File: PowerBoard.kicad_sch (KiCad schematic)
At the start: 113 parts, among them J1 XT90, J10 DEAN_T, J11 DEAN_T, J12 DEAN_T, J13 DEAN_T, J14 DEAN_T, J15 DEAN_T, J16 XT60, J17 XT60, J18 XT60, J19 XT60, J2 DEAN_T, J20 XT60, J21 XT60, J22 XT30, J23 XT30, J24 XT30, J25 XT30, J26 XT30, J27 XT30, J28 XT90, J29 XT30, J3 XT60, J30 XT30, J31 XT30, J32 Conn_01x02, J4 XT30, J5 XT90, J6 XT90, J7 XT90, J8 XT90, J9 XT90, Q1 IRF9540N, Q2 IRF9540N, Q3 BC817, Q4 BC817, Q5 IRF9540N, Q6 BC817, Q7 IRF9540N, Q8 BC817, U1 Pico, U2 LM317_TO-220

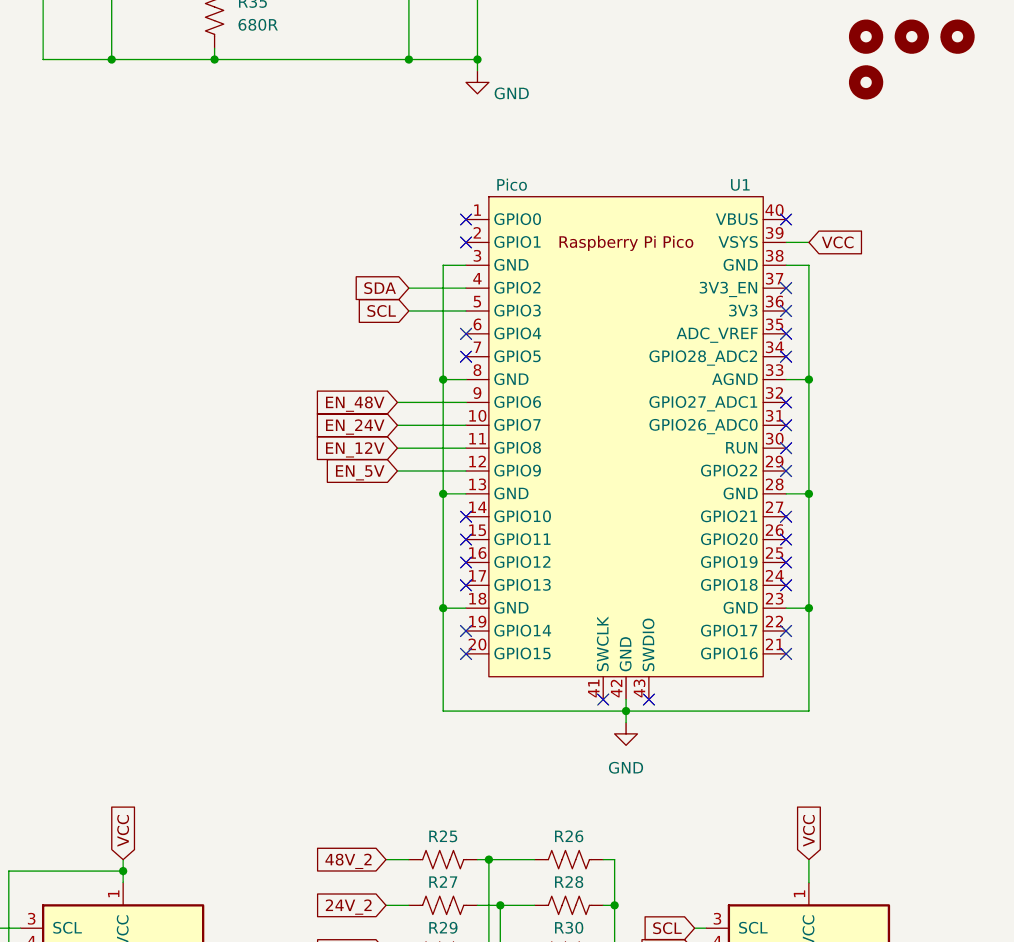
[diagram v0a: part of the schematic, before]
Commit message: added status leds
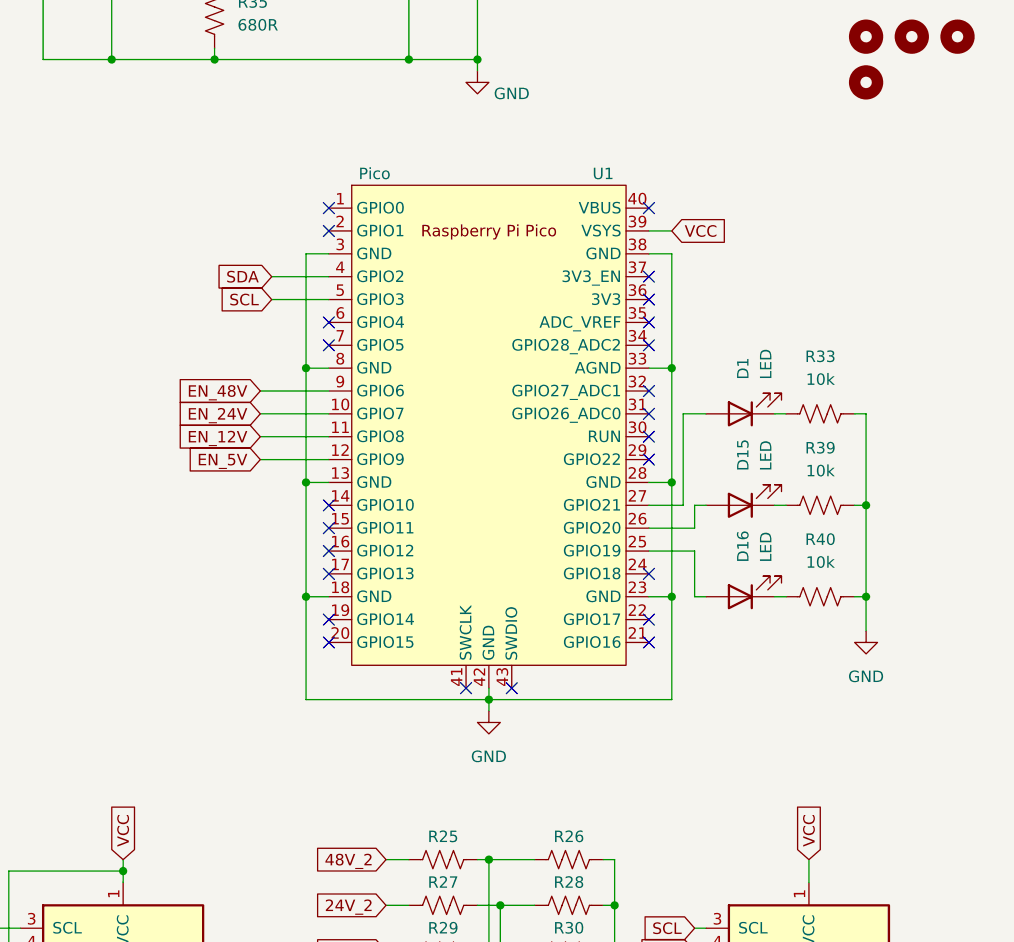
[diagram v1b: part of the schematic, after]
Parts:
- added D1, D15, D16: LED, Diode_SMD:D_1206_3216Metric, symbol Device:LED
- added R33, R39, R40: 10k, Resistor_SMD:R_1206_3216Metric, symbol Device:R_US
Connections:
- net GND: now also R33.2, R39.2, R40.2
- net at U1.25 (GPIO19): now also D16.2 (A)
- net at U1.26 (GPIO20): now also D15.2 (A)
- net at U1.27 (GPIO21): now also D1.2 (A)
- new net: D15.1 (K), R39.1
- new net: D16.1 (K), R40.1
- new net: D1.1 (K), R33.1
- no-connect marks 29 -> 26
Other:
- moved on the sheet: U1

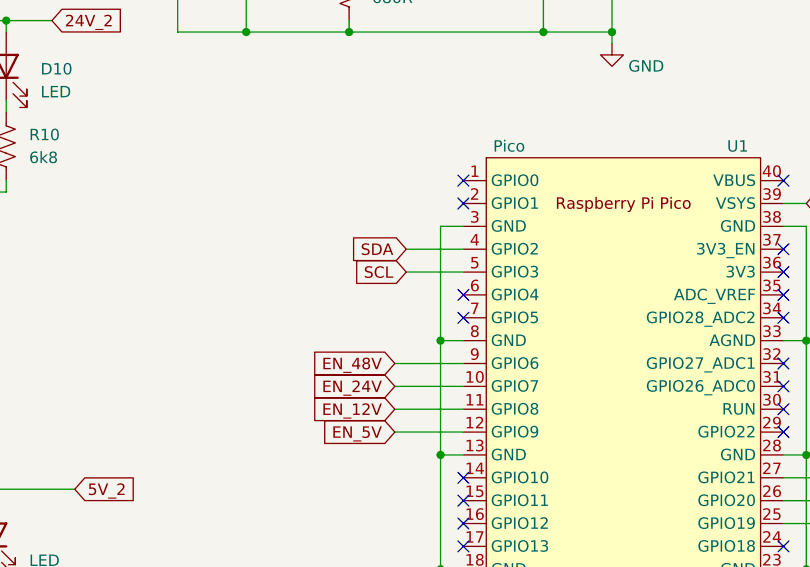
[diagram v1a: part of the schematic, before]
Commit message: changed i2c connection
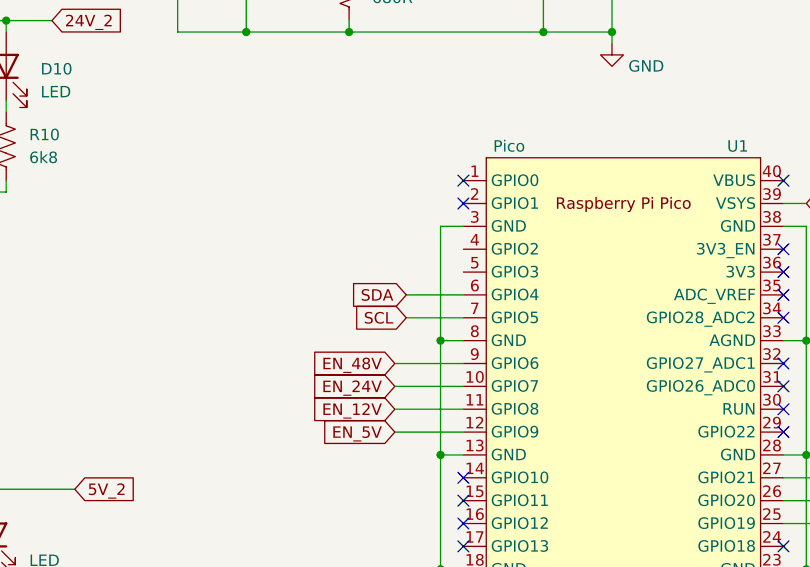
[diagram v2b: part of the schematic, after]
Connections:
- net SCL: now also U1.7 (GPIO5); no longer U1.5 (GPIO3)
- net SDA: now also U1.6 (GPIO4); no longer U1.4 (GPIO2)
- no-connect marks 26 -> 24
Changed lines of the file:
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@@
 	)
 	(no_connect
-		(at 208.28 71.12)
-	)
-	(no_connect
 		(at 243.84 104.14)
 	)
 	(no_connect
-		(at 208.28 68.58)
-	)
-	(no_connect
 		(at 243.84 76.2)
 	)
@@
 	(wire
 		(pts
-			(xy 201.93 66.04) (xy 208.28 66.04)
-		)
-		(stroke
-			(width 0)
-			(type default)
-		)
-	)
-	(wire
-		(pts
 			(xy 124.46 73.66) (xy 124.46 80.01)
 		)
@@
 	(wire
 		(pts
+			(xy 201.93 68.58) (xy 208.28 68.58)
+		)
+		(stroke
+			(width 0)
+			(type default)
+		)
+	)
+	(wire
+		(pts
 			(xy 205.74 110.49) (xy 226.06 110.49)
 		)
@@
 	(wire
 		(pts
-			(xy 201.93 63.5) (xy 208.28 63.5)
-		)
-		(stroke
-			(width 0)
-			(type default)
-		)
-	)
-	(wire
-		(pts
 			(xy 143.51 90.17) (xy 143.51 91.44)
 		)
@@
 	(wire
 		(pts
+			(xy 201.93 71.12) (xy 208.28 71.12)
+		)
+		(stroke
+			(width 0)
+			(type default)
+		)
+	)
+	(wire
+		(pts
 			(xy 44.45 27.94) (xy 41.91 27.94)
 		)
@@
 	(global_label "SCL"
 		(shape input)
-		(at 201.93 66.04 180)
+		(at 201.93 71.12 180)
 		(fields_autoplaced yes)
 		(effects
@@
 		)
 		(property "Intersheetrefs" "${INTERSHEET_REFS}"
-			(at 195.4372 66.04 0)
+			(at 195.4372 71.12 0)
 			(effects
 				(font
@@
 	(global_label "SDA"
 		(shape input)
-		(at 201.93 63.5 180)
+		(at 201.93 68.58 180)
 		(fields_autoplaced yes)
 		(effects
@@
 		)
 		(property "Intersheetrefs" "${INTERSHEET_REFS}"
-			(at 195.3767 63.5 0)
+			(at 195.3767 68.58 0)
 			(effects
 				(font

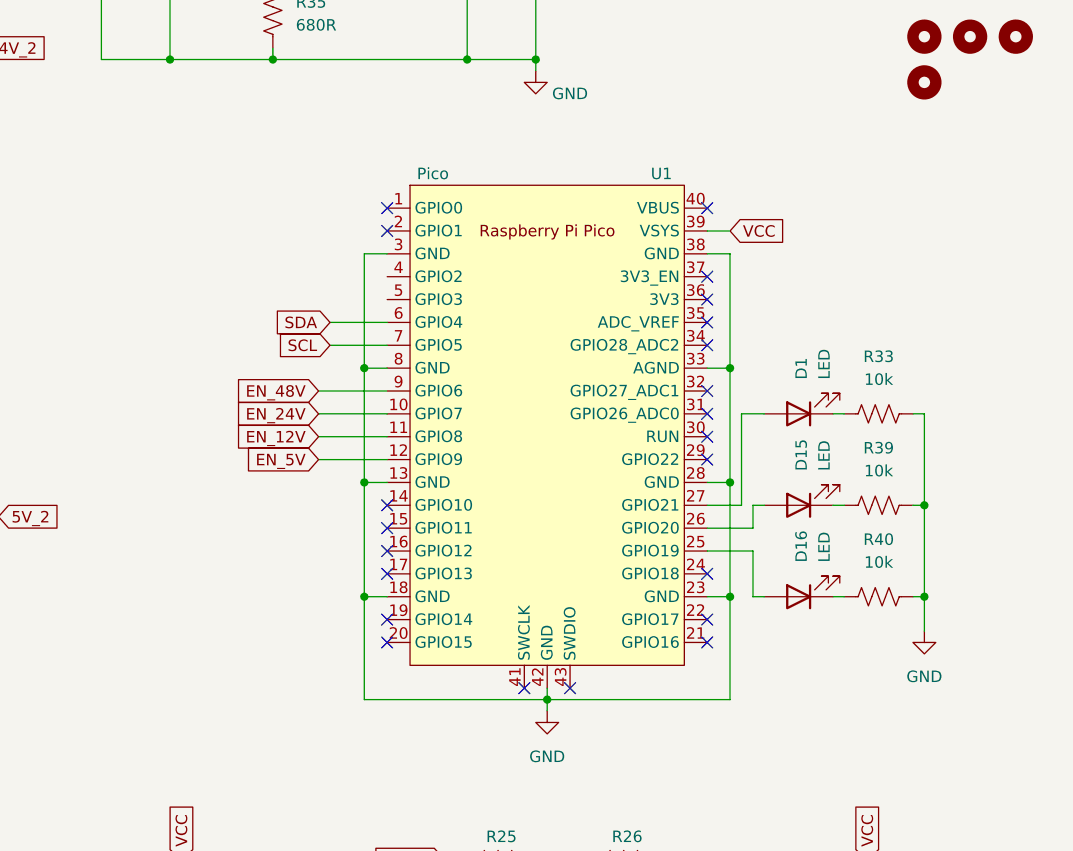
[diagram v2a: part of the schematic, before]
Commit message: added spi and i2c terminals
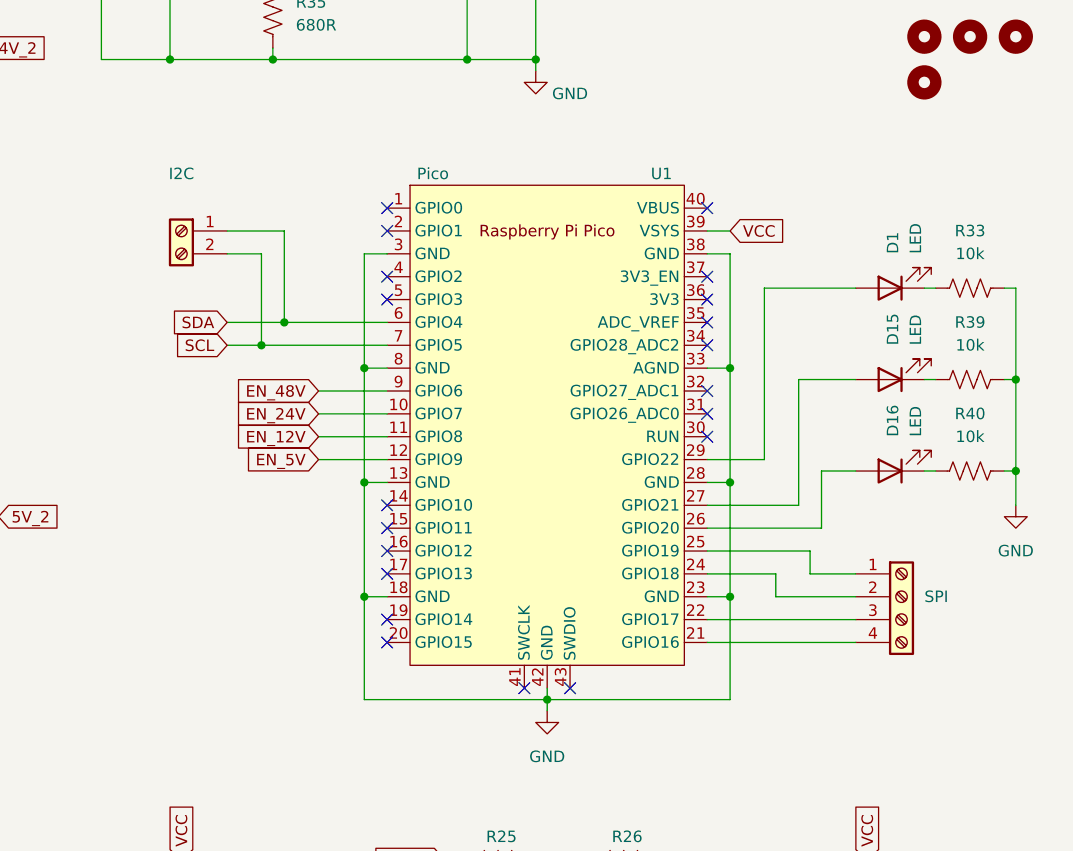
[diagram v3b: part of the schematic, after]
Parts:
- added I2C: Screw_Terminal_01x02, TerminalBlock:TerminalBlock_Xinya_XY308-2.54-2P_1x02_P2.54mm_Horizontal, symbol Connector:Screw_Terminal_01x02
- added SPI: Screw_Terminal_01x04, TerminalBlock:TerminalBlock_Xinya_XY308-2.54-4P_1x04_P2.54mm_Horizontal, symbol Connector:Screw_Terminal_01x04
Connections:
- net SCL: now also I2C.2 (Pin_2)
- net SDA: now also I2C.1 (Pin_1)
- net at D15.2 (A): now also U1.27 (GPIO21); no longer U1.26 (GPIO20)
- net at U1.21 (GPIO16): now also SPI.4 (Pin_4)
- net at U1.22 (GPIO17): now also SPI.3 (Pin_3)
- net at U1.24 (GPIO18): now also SPI.2 (Pin_2)
- net at U1.25 (GPIO19): now also SPI.1 (Pin_1); no longer D16.2 (A)
- net at D1.2 (A): now also U1.29 (GPIO22); no longer U1.27 (GPIO21)
- new net: D16.2 (A), U1.26 (GPIO20)
- no-connect marks 24 -> 22
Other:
- moved on the sheet: D1, D15, D16, R33, R39, R40

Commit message: sync
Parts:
- renumbered I2C to I2C1, SPI to SPI1
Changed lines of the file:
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@@
 		(dnp no)
 		(fields_autoplaced yes)
-		(property "Reference" "SPI"
+		(property "Reference" "SPI1"
 			(at 267.97 99.0599 0)
 			(effects
@@
 			(project ""
 				(path "/0dc459cd-c845-409c-9d50-e420f03142d8"
-					(reference "SPI")
+					(reference "SPI1")
 					(unit 1)
 				)
@@
 		(dnp no)
 		(fields_autoplaced yes)
-		(property "Reference" "I2C"
+		(property "Reference" "I2C1"
 			(at 185.42 52.07 0)
 			(effects
@@
 			(project ""
 				(path "/0dc459cd-c845-409c-9d50-e420f03142d8"
-					(reference "I2C")
+					(reference "I2C1")
 					(unit 1)
 				)

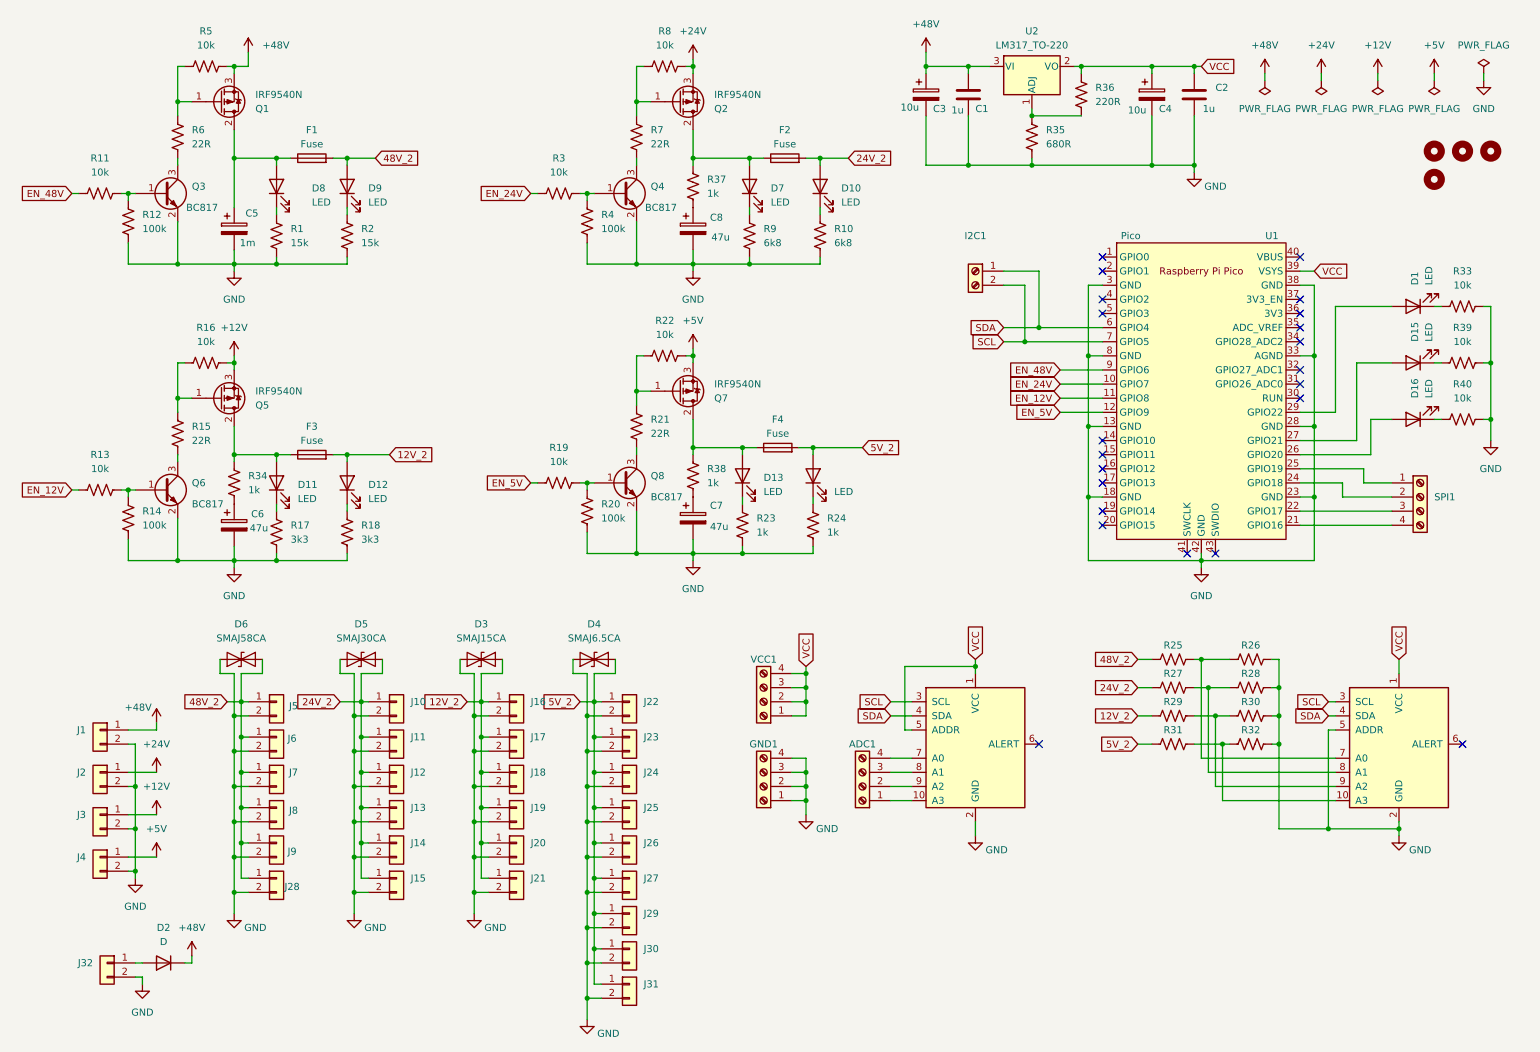
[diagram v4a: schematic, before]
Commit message: Remove unused switch on the battery rail
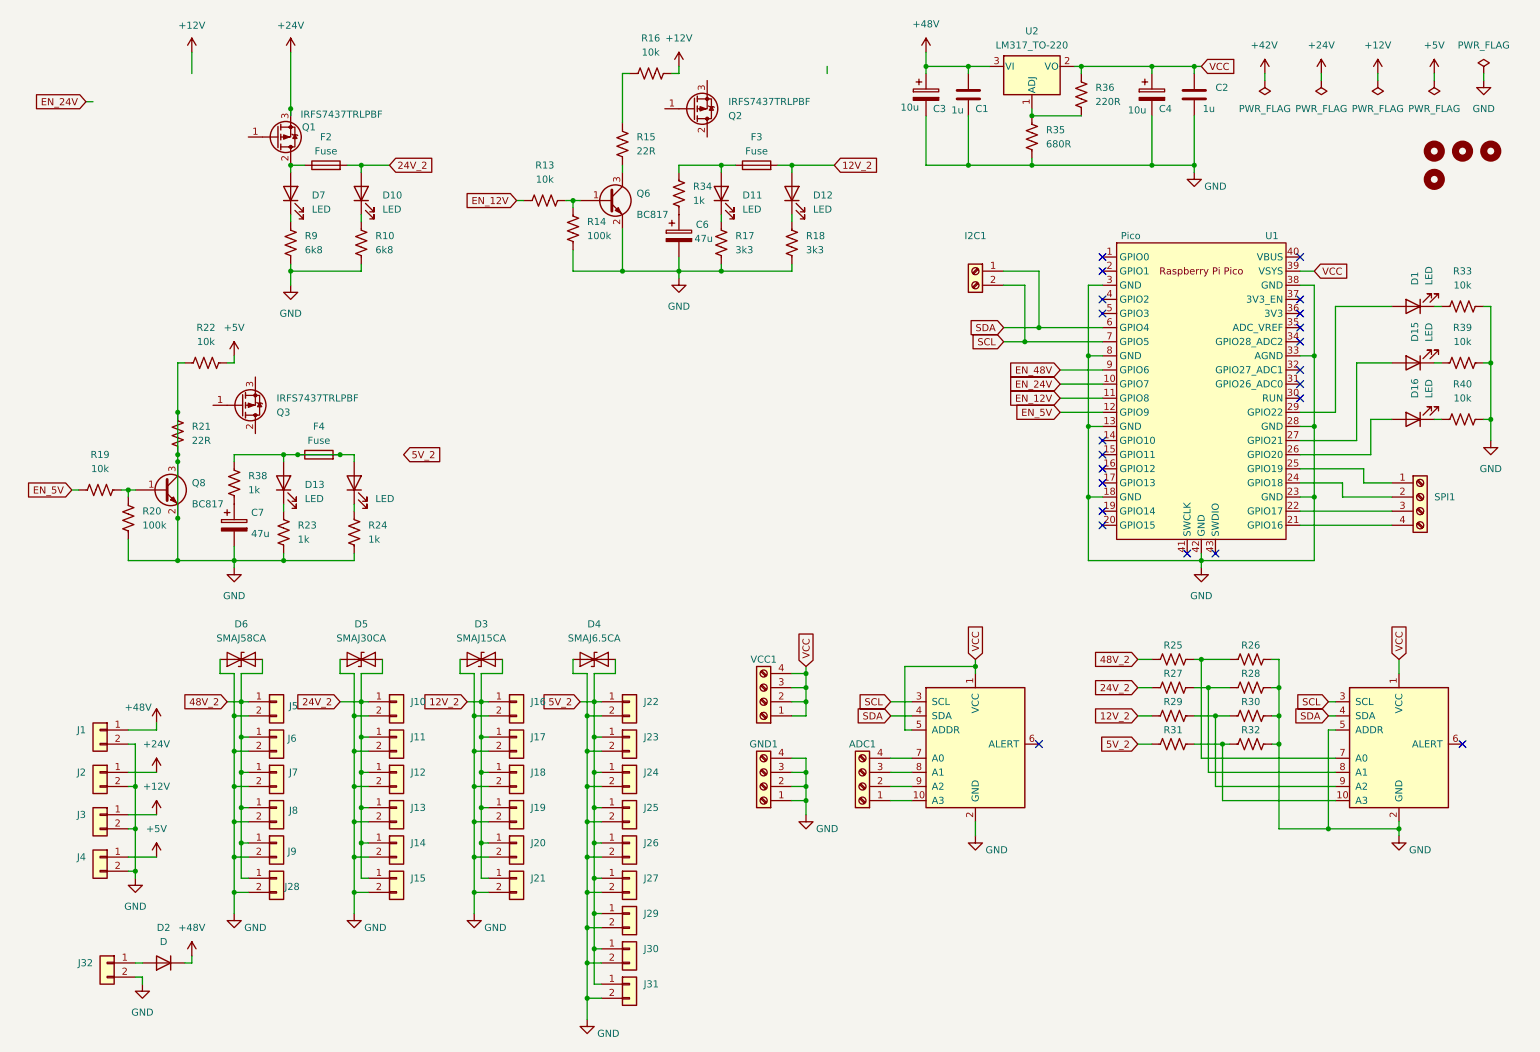
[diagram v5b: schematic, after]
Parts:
- removed C5: 1m, Capacitor_THT:CP_Radial_D16.0mm_P7.50mm, symbol Device:C_Polarized
- removed C8: 47u, Capacitor_THT:CP_Radial_D6.3mm_P2.50mm, symbol Device:C_Polarized
- removed D8, D9: LED, Diode_SMD:D_1206_3216Metric, symbol Device:LED
- removed F1: Fuse, Fuse:Fuse_Blade_ATO_directSolder, symbol Device:Fuse
- removed Q3, Q4: BC817, Package_TO_SOT_SMD:SOT-23, symbol Transistor_BJT:BC817
- removed Q5, Q7: IRF9540N, Package_TO_SOT_THT:TO-220-3_Vertical, symbol Transistor_FET:IRF9540N
- removed R1, R2: 15k, Resistor_SMD:R_1206_3216Metric, symbol Device:R_US
- removed R11, R3, R5, R8: 10k, Resistor_SMD:R_1206_3216Metric, symbol Device:R_US
- removed R12, R4: 100k, Resistor_SMD:R_1206_3216Metric, symbol Device:R_US
- removed R37: 1k, Resistor_SMD:R_1206_3216Metric, symbol Device:R_US
- removed R6, R7: 22R, Resistor_SMD:R_1206_3216Metric, symbol Device:R_US
- added Q3: IRFS7437TRLPBF, Package_TO_SOT_SMD:TO-263-2, symbol Transistor_FET:IRF9540N
- Q1, Q2: value IRF9540N -> IRFS7437TRLPBF; footprint Package_TO_SOT_THT:TO-220-3_Vertical -> Package_TO_SOT_SMD:TO-263-2
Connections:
- net +24V: now also Q1.3 (S); no longer Q2.3 (S)
- net +48V: no longer Q1.3 (S)
- net 5V_2: no longer D14.2 (A), F4.2
- net GND: now also Q8.3 (C), R21.1, R21.2, R22.1
- net at D13.2 (A), F4.1, R38.1: now also D14.2 (A), F4.2
- net at Q1.2 (D): now also D7.2 (A), F2.1
- now unconnected: Q2.2 (D)
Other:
- moved on the sheet: C6, C7, D10, D11, D12, D13, D7, F2, F3, F4, Q2, Q6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
